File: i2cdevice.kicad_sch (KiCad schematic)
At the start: 46 parts, among them J29 6x2.54mm, J30 6x2.54mm, J31 6x2.54mm, J32 6x2.54mm, U10 INA219AxD, U11 MCP4725xxx-xCH, U12 24LC32

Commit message: First try to fit electronic on PCB
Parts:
- removed TP189: TestPoint_Small, Connector_PinHeader_2.54mm:PinHeader_1x01_P2.54mm_Horizontal, symbol Connector:TestPoint_Small
- TP100: renamed from TP215; footprint Connector_PinHeader_2.54mm:PinHeader_1x01_P2.54mm_Horizontal -> Connector_Pin:Pin_D1.0mm_L10.0mm
- TP101: renamed from TP216; footprint Connector_PinHeader_2.54mm:PinHeader_1x01_P2.54mm_Horizontal -> Connector_Pin:Pin_D1.0mm_L10.0mm
- U10: footprint Package_SO:SOIC-8_3.9x4.9mm_P1.27mm -> Package_TO_SOT_SMD:SOT-23-8; symbol Analog_ADC:INA219AxD -> Analog_ADC:INA219AxDCN
- renumbered J29 to J30, J30 to J31, J31 to J32, J32 to J33, NT459 to NT471, NT460 to NT472, NT461 to NT473, NT462 to NT474, NT463 to NT475, NT464 to NT476, NT465 to NT477, NT466 to NT478, NT467 to NT479, NT468 to NT480, NT469 to NT481, NT470 to NT482, NT471 to NT483, NT472 to NT484, NT473 to NT485, NT474 to NT486, NT475 to NT487, NT586 to NT488, NT476 to NT489, NT587 to NT490, NT477 to NT491, NT478 to NT492, NT479 to NT493, R86 to R73, R87 to R74, R88 to R75, R89 to R76, R90 to R77, R91 to R78, R92 to R79, R93 to R80, R94 to R81, R95 to R82, R96 to R83
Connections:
- net GND: now also U10.3 (GND); no longer U10.6 (GND)
- net I2C0_SCL: now also NT473.1; no longer NT471.1
- net I2C0_SDA: now also NT471.1; no longer NT473.1
- net I_SCL: now also NT473.2, R73.1, U10.5 (SCL); no longer NT471.2, R74.1, U10.3 (SDA)
- net I_SDA: now also NT471.2, R74.1, U10.6 (SDA); no longer NT473.2, R73.1, U10.4 (SCL)
- net VCC: now also U10.4 (VS); no longer U10.5 (VS)
- net VIN+: now also U10.1 (IN+); no longer U10.8 (IN+)
- net VIN-: now also U10.2 (IN-); no longer U10.7 (IN-)
- net at R79.1, R82.2: now also U10.7 (A0); no longer U10.2 (A0)
- net at R78.1, R81.2: now also U10.8 (A1); no longer U10.1 (A1)

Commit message: backup 1 bank done
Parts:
- NT471, NT472, NT473, NT474, NT475, NT476, NT477, NT478, NT479, NT480, NT481, NT482, NT483, NT484, NT485, NT486, NT487, NT488, NT489, NT490, NT491, NT492, NT493: footprint NetTie:NetTie-2_THT_Pad1.0mm -> NetTie:NetTie-2_Front1.0mm
- TP100, TP101: footprint Connector_Pin:Pin_D1.0mm_L10.0mm -> Connector_Pin:Pin_D0.9mm_L10.0mm_W2.4mm_FlatFork
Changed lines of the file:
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@@
     (property "Reference" "NT476" (id 0) (at 248.92 58.42 0))
     (property "Value" "I_INH" (id 1) (at 248.92 60.96 0))
-    (property "Footprint" "NetTie:NetTie-2_THT_Pad1.0mm" (id 2) (at 248.92 59.69 0)
+    (property "Footprint" "NetTie:NetTie-2_Front1.0mm" (id 2) (at 248.92 59.69 0)
       (effects (font (size 1.27 1.27)) hide)
     )
@@
     (property "Reference" "NT485" (id 0) (at 116.84 140.97 0))
     (property "Value" "C_M2" (id 1) (at 116.84 143.51 0))
-    (property "Footprint" "NetTie:NetTie-2_THT_Pad1.0mm" (id 2) (at 116.84 142.24 0)
+    (property "Footprint" "NetTie:NetTie-2_Front1.0mm" (id 2) (at 116.84 142.24 0)
       (effects (font (size 1.27 1.27)) hide)
     )
@@
     (property "Reference" "NT481" (id 0) (at 107.95 138.43 0))
     (property "Value" "C_M1" (id 1) (at 107.95 140.97 0))
-    (property "Footprint" "NetTie:NetTie-2_THT_Pad1.0mm" (id 2) (at 107.95 139.7 0)
+    (property "Footprint" "NetTie:NetTie-2_Front1.0mm" (id 2) (at 107.95 139.7 0)
       (effects (font (size 1.27 1.27)) hide)
     )
@@
     (property "Reference" "NT492" (id 0) (at 52.07 148.59 0))
     (property "Value" "C_VCC" (id 1) (at 52.07 151.13 0))
-    (property "Footprint" "NetTie:NetTie-2_THT_Pad1.0mm" (id 2) (at 52.07 149.86 0)
+    (property "Footprint" "NetTie:NetTie-2_Front1.0mm" (id 2) (at 52.07 149.86 0)
       (effects (font (size 1.27 1.27)) hide)
     )
@@
     (property "Reference" "NT474" (id 0) (at 179.07 55.88 0))
     (property "Value" "D_SDA" (id 1) (at 179.07 58.42 0))
-    (property "Footprint" "NetTie:NetTie-2_THT_Pad1.0mm" (id 2) (at 179.07 57.15 0)
+    (property "Footprint" "NetTie:NetTie-2_Front1.0mm" (id 2) (at 179.07 57.15 0)
       (effects (font (size 1.27 1.27)) hide)
     )
@@
     (property "Reference" "NT480" (id 0) (at 50.8 138.43 0))
     (property "Value" "C_SDA" (id 1) (at 50.8 140.97 0))
-    (property "Footprint" "NetTie:NetTie-2_THT_Pad1.0mm" (id 2) (at 50.8 139.7 0)
+    (property "Footprint" "NetTie:NetTie-2_Front1.0mm" (id 2) (at 50.8 139.7 0)
       (effects (font (size 1.27 1.27)) hide)
     )
@@
     (property "Reference" "NT491" (id 0) (at 116.84 146.05 0))
     (property "Value" "C_M4" (id 1) (at 116.84 148.59 0))
-    (property "Footprint" "NetTie:NetTie-2_THT_Pad1.0mm" (id 2) (at 116.84 147.32 0)
+    (property "Footprint" "NetTie:NetTie-2_Front1.0mm" (id 2) (at 116.84 147.32 0)
       (effects (font (size 1.27 1.27)) hide)
     )
@@
     (property "Reference" "NT477" (id 0) (at 127 62.23 0))
     (property "Value" "I_INL" (id 1) (at 127 64.77 0))
-    (property "Footprint" "NetTie:NetTie-2_THT_Pad1.0mm" (id 2) (at 127 63.5 0)
+    (property "Footprint" "NetTie:NetTie-2_Front1.0mm" (id 2) (at 127 63.5 0)
       (effects (font (size 1.27 1.27)) hide)
     )
@@
     (property "Reference" "NT482" (id 0) (at 200.66 138.43 0))
     (property "Value" "EE_A1" (id 1) (at 200.66 140.97 0))
-    (property "Footprint" "NetTie:NetTie-2_THT_Pad1.0mm" (id 2) (at 200.66 139.7 0)
+    (property "Footprint" "NetTie:NetTie-2_Front1.0mm" (id 2) (at 200.66 139.7 0)
       (effects (font (size 1.27 1.27)) hide)
     )
@@
     (property "Reference" "NT493" (id 0) (at 60.96 151.13 0))
     (property "Value" "C_GND" (id 1) (at 60.96 153.67 0))
-    (property "Footprint" "NetTie:NetTie-2_THT_Pad1.0mm" (id 2) (at 60.96 152.4 0)
+    (property "Footprint" "NetTie:NetTie-2_Front1.0mm" (id 2) (at 60.96 152.4 0)
       (effects (font (size 1.27 1.27)) hide)
     )
@@
     (property "Reference" "NT471" (id 0) (at 44.45 53.34 0))
     (property "Value" "I_SDA" (id 1) (at 44.45 55.88 0))
-    (property "Footprint" "NetTie:NetTie-2_THT_Pad1.0mm" (id 2) (at 44.45 54.61 0)
+    (property "Footprint" "NetTie:NetTie-2_Front1.0mm" (id 2) (at 44.45 54.61 0)
       (effects (font (size 1.27 1.27)) hide)
     )
@@
     (property "Reference" "NT484" (id 0) (at 43.18 140.97 0))
     (property "Value" "C_SCL" (id 1) (at 43.18 143.51 0))
-    (property "Footprint" "NetTie:NetTie-2_THT_Pad1.0mm" (id 2) (at 43.18 142.24 0)
+    (property "Footprint" "NetTie:NetTie-2_Front1.0mm" (id 2) (at 43.18 142.24 0)
       (effects (font (size 1.27 1.27)) hide)
     )
@@
     (property "Reference" "NT479" (id 0) (at 232.41 135.89 0))
     (property "Value" "EE_SDA" (id 1) (at 232.41 138.43 0))
-    (property "Footprint" "NetTie:NetTie-2_THT_Pad1.0mm" (id 2) (at 232.41 137.16 0)
+    (property "Footprint" "NetTie:NetTie-2_Front1.0mm" (id 2) (at 232.41 137.16 0)
       (effects (font (size 1.27 1.27)) hide)
     )
@@
       (effects (font (size 1.27 1.27)) (justify left) hide)
     )
-    (property "Footprint" "Connector_Pin:Pin_D1.0mm_L10.0mm" (id 2) (at 113.03 157.48 0)
+    (property "Footprint" "Connector_Pin:Pin_D0.9mm_L10.0mm_W2.4mm_FlatFork" (id 2) (at 113.03 157.48 0)
       (effects (font (size 1.27 1.27)) hide)
     )
@@
     (property "Reference" "NT489" (id 0) (at 107.95 143.51 0))
     (property "Value" "C_M3" (id 1) (at 107.95 146.05 0))
-    (property "Footprint" "NetTie:NetTie-2_THT_Pad1.0mm" (id 2) (at 107.95 144.78 0)
+    (property "Footprint" "NetTie:NetTie-2_Front1.0mm" (id 2) (at 107.95 144.78 0)
       (effects (font (size 1.27 1.27)) hide)
     )
@@
     (property "Reference" "NT490" (id 0) (at 43.18 146.05 0))
     (property "Value" "C_4" (id 1) (at 43.18 148.59 0))
-    (property "Footprint" "NetTie:NetTie-2_THT_Pad1.0mm" (id 2) (at 43.18 147.32 0)
+    (property "Footprint" "NetTie:NetTie-2_Front1.0mm" (id 2) (at 43.18 147.32 0)
       (effects (font (size 1.27 1.27)) hide)
     )
@@
     (property "Reference" "NT488" (id 0) (at 50.8 143.51 0))
     (property "Value" "C_3" (id 1) (at 50.8 146.05 0))
-    (property "Footprint" "NetTie:NetTie-2_THT_Pad1.0mm" (id 2) (at 50.8 144.78 0)
+    (property "Footprint" "NetTie:NetTie-2_Front1.0mm" (id 2) (at 50.8 144.78 0)
       (effects (font (size 1.27 1.27)) hide)
     )
@@
     (property "Reference" "NT478" (id 0) (at 191.77 135.89 0))
     (property "Value" "EE_A0" (id 1) (at 191.77 138.43 0))
-    (property "Footprint" "NetTie:NetTie-2_THT_Pad1.0mm" (id 2) (at 191.77 137.16 0)
+    (property "Footprint" "NetTie:NetTie-2_Front1.0mm" (id 2) (at 191.77 137.16 0)
       (effects (font (size 1.27 1.27)) hide)
     )
@@
     (property "Reference" "NT487" (id 0) (at 233.68 140.97 0))
     (property "Value" "EE_A2" (id 1) (at 233.68 143.51 0))
-    (property "Footprint" "NetTie:NetTie-2_THT_Pad1.0mm" (id 2) (at 233.68 142.24 0)
+    (property "Footprint" "NetTie:NetTie-2_Front1.0mm" (id 2) (at 233.68 142.24 0)
       (effects (font (size 1.27 1.27)) hide)
     )
@@
     (property "Reference" "NT475" (id 0) (at 171.45 58.42 0))
     (property "Value" "D_SCL" (id 1) (at 171.45 60.96 0))
-    (property "Footprint" "NetTie:NetTie-2_THT_Pad1.0mm" (id 2) (at 171.45 59.69 0)
+    (property "Footprint" "NetTie:NetTie-2_Front1.0mm" (id 2) (at 171.45 59.69 0)
       (effects (font (size 1.27 1.27)) hide)
     )
@@
     (property "Reference" "NT473" (id 0) (at 36.83 55.88 0))
     (property "Value" "I_SCL" (id 1) (at 36.83 58.42 0))
-    (property "Footprint" "NetTie:NetTie-2_THT_Pad1.0mm" (id 2) (at 36.83 57.15 0)
+    (property "Footprint" "NetTie:NetTie-2_Front1.0mm" (id 2) (at 36.83 57.15 0)
       (effects (font (size 1.27 1.27)) hide)
     )
@@
     (property "Reference" "NT483" (id 0) (at 240.03 138.43 0))
     (property "Value" "EE_SCL" (id 1) (at 240.03 140.97 0))
-    (property "Footprint" "NetTie:NetTie-2_THT_Pad1.0mm" (id 2) (at 240.03 139.7 0)
+    (property "Footprint" "NetTie:NetTie-2_Front1.0mm" (id 2) (at 240.03 139.7 0)
       (effects (font (size 1.27 1.27)) hide)
     )
@@
       (effects (font (size 1.27 1.27)) (justify left) hide)
     )
-    (property "Footprint" "Connector_Pin:Pin_D1.0mm_L10.0mm" (id 2) (at 113.03 152.4 0)
+    (property "Footprint" "Connector_Pin:Pin_D0.9mm_L10.0mm_W2.4mm_FlatFork" (id 2) (at 113.03 152.4 0)
       (effects (font (size 1.27 1.27)) hide)
     )
@@
     (property "Reference" "NT472" (id 0) (at 127 54.61 0))
     (property "Value" "I_INH" (id 1) (at 127 57.15 0))
-    (property "Footprint" "NetTie:NetTie-2_THT_Pad1.0mm" (id 2) (at 127 55.88 0)
+    (property "Footprint" "NetTie:NetTie-2_Front1.0mm" (id 2) (at 127 55.88 0)
       (effects (font (size 1.27 1.27)) hide)
     )
@@
     (property "Reference" "NT486" (id 0) (at 191.77 140.97 0))
     (property "Value" "EE_A2" (id 1) (at 191.77 143.51 0))
-    (property "Footprint" "NetTie:NetTie-2_THT_Pad1.0mm" (id 2) (at 191.77 142.24 0)
-      (effects (font (size 1.27 1.27)) hide)
-    )
+    (property "Footprint" "NetTie:NetTie-2_Front1.0mm" (id 2) (at 191.77 142.24 0)
+      (effects (font (size 1.27 1.27)) hide)
+    )

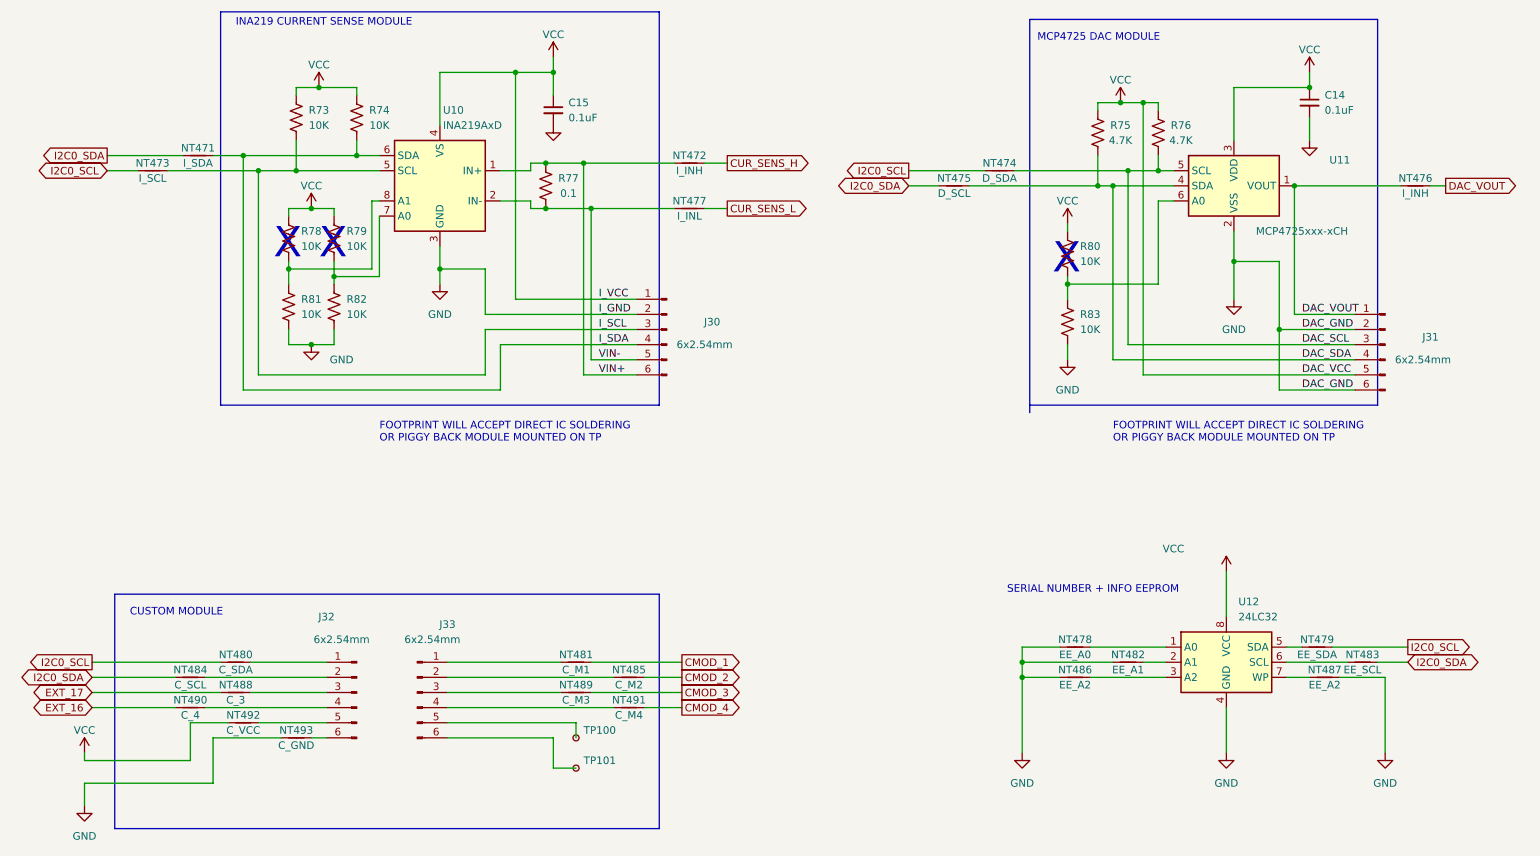
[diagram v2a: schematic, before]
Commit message: PCB Completed
PCB completed but final verification not completed
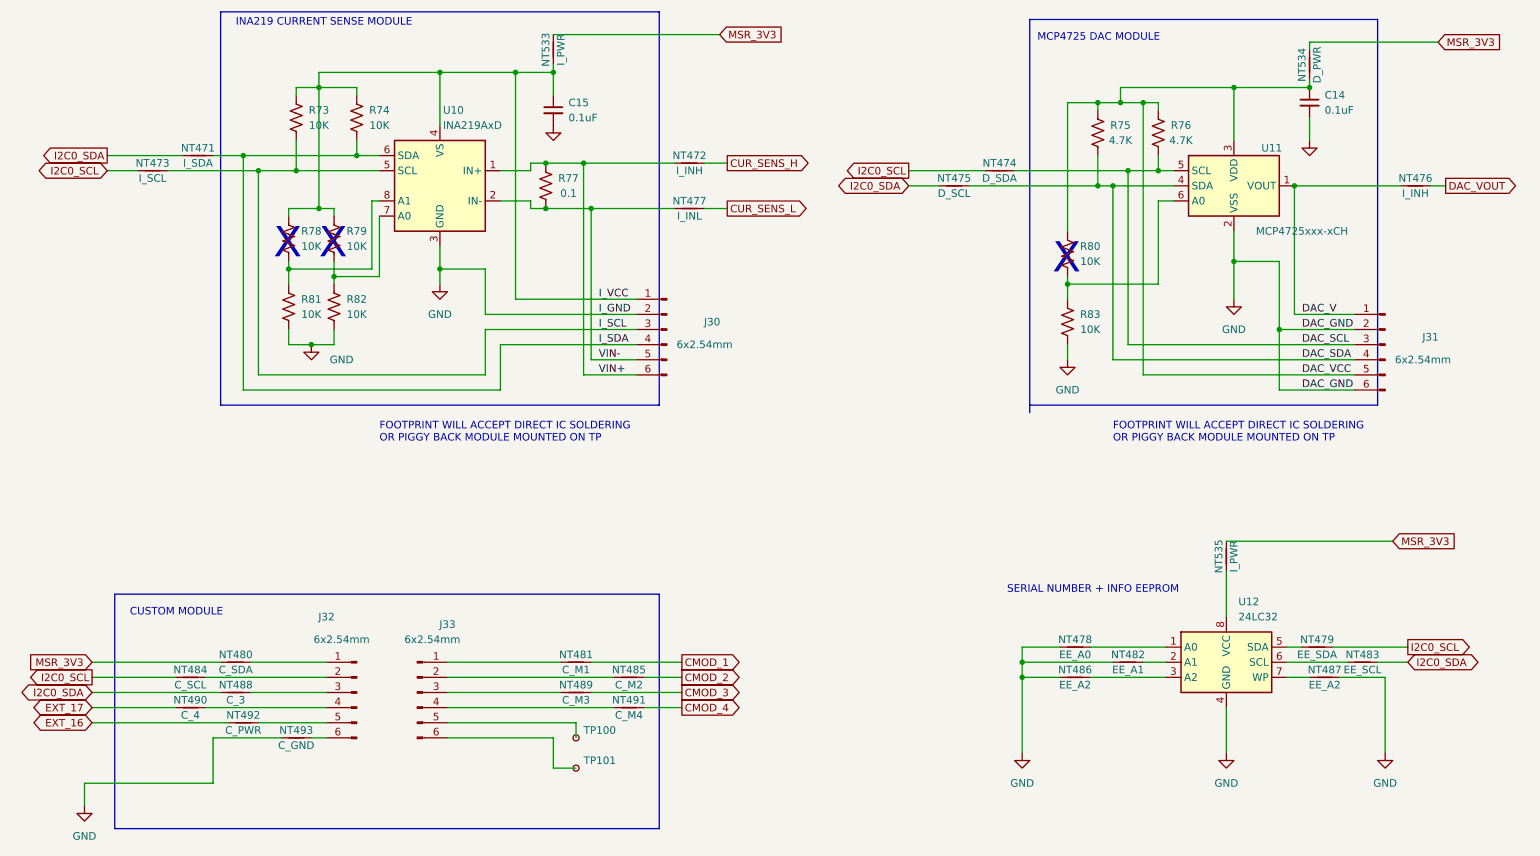
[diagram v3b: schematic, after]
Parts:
- added NT533, NT535: I_PWR, NetTie:NetTie-2_Front1.0mm, symbol Device:NetTie_2
- added NT534: D_PWR, NetTie:NetTie-2_Front1.0mm, symbol Device:NetTie_2
- J30, J31, J32, J33: footprint Connector_PinHeader_2.54mm:PinHeader_1x06_P2.54mm_Vertical -> Connector_PinSocket_2.54mm:PinSocket_1x06_P2.54mm_Vertical
- NT492: value C_VCC -> C_PWR
- TP100, TP101: footprint Connector_Pin:Pin_D0.9mm_L10.0mm_W2.4mm_FlatFork -> TestPoint:TestPoint_THTPad_D1.5mm_Drill0.7mm
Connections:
- net DAC_VOUT: no longer J31.1 (Pin_1), NT476.2, U11.1 (VOUT)
- net EXT_16: now also NT492.1; no longer NT490.1
- net EXT_17: now also NT490.1; no longer NT488.1
- net I2C0_SCL: now also NT484.1; no longer NT480.1
- net I2C0_SDA: now also NT488.1; no longer NT484.1
- removed net VCC: C14.1, C15.1, J30.1 (Pin_1), J31.5 (Pin_5), NT492.1, R73.2, R74.2, R75.2, R76.2, R78.2, R79.2, R80.2, U10.4 (VS), U11.3 (VDD), U12.8 (VCC)
- new net: NT535.1, U12.8 (VCC)
- new net DAC_V: J31.1 (Pin_1), NT476.2, U11.1 (VOUT)
- new net DAC_VCC: C14.1, J31.5 (Pin_5), NT534.1, R75.2, R76.2, R80.2, U11.3 (VDD)
- new net I_VCC: C15.1, J30.1 (Pin_1), NT533.1, R73.2, R74.2, R78.2, R79.2, U10.4 (VS)
- new net MSR_3V3: NT480.1, NT533.2, NT534.2, NT535.2

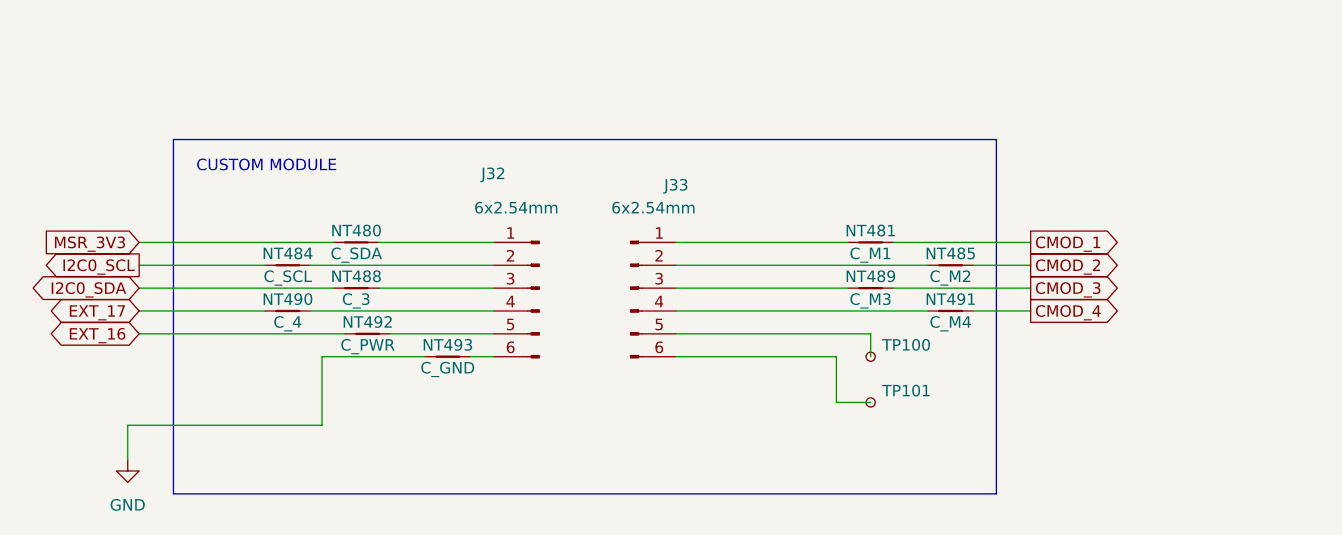
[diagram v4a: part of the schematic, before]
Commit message: Change custom connector
Use 8 pins to replace 6 pins
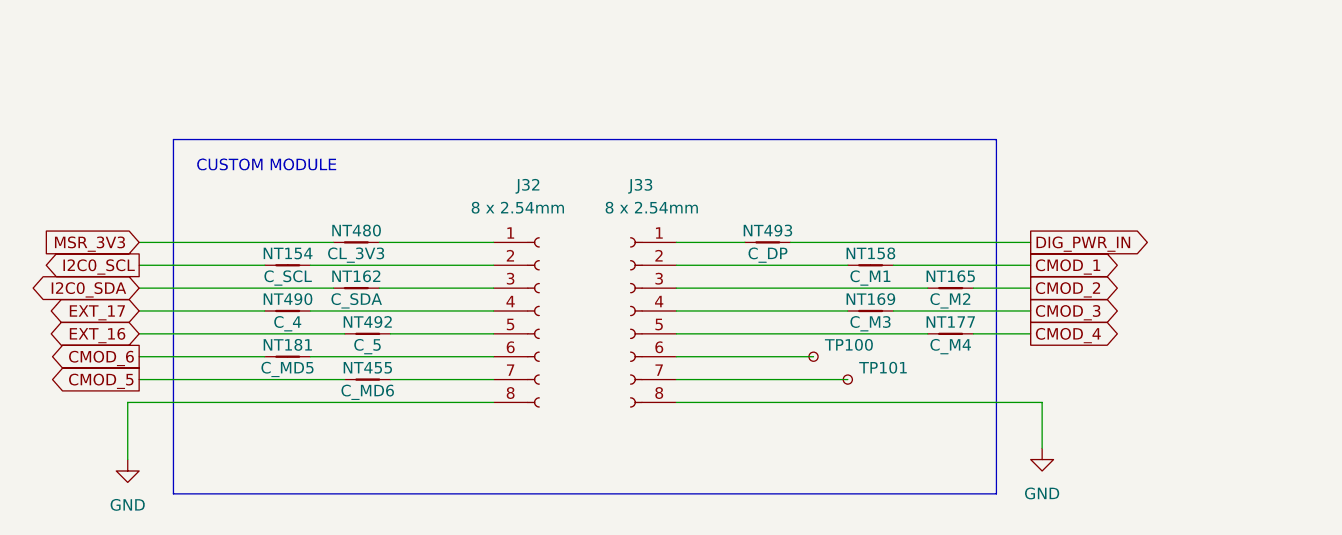
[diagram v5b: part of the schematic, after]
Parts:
- removed J32, J33: 6x2.54mm, Connector_PinSocket_2.54mm:PinSocket_1x06_P2.54mm_Vertical, symbol Connector:Conn_01x06_Male
- removed NT481: C_M1, NetTie:NetTie-2_Front1.0mm, symbol Device:NetTie_2
- removed NT484: C_SCL, NetTie:NetTie-2_Front1.0mm, symbol Device:NetTie_2
- removed NT485: C_M2, NetTie:NetTie-2_Front1.0mm, symbol Device:NetTie_2
- removed NT488: C_3, NetTie:NetTie-2_Front1.0mm, symbol Device:NetTie_2
- removed NT489: C_M3, NetTie:NetTie-2_Front1.0mm, symbol Device:NetTie_2
- removed NT491: C_M4, NetTie:NetTie-2_Front1.0mm, symbol Device:NetTie_2
- added J32, J33: 8 x 2.54mm, Connector_PinSocket_2.54mm:PinSocket_1x08_P2.54mm_Vertical, symbol Connector:Conn_01x08_Female
- added NT154: C_SCL, NetTie:NetTie-2_Front1.0mm, symbol Device:NetTie_2
- added NT158: C_M1, NetTie:NetTie-2_Front1.0mm, symbol Device:NetTie_2
- added NT162: C_SDA, NetTie:NetTie-2_Front1.0mm, symbol Device:NetTie_2
- added NT165: C_M2, NetTie:NetTie-2_Front1.0mm, symbol Device:NetTie_2
- added NT169: C_M3, NetTie:NetTie-2_Front1.0mm, symbol Device:NetTie_2
- added NT177: C_M4, NetTie:NetTie-2_Front1.0mm, symbol Device:NetTie_2
- added NT181: C_MD5, NetTie:NetTie-2_Front1.0mm, symbol Device:NetTie_2
- added NT455: C_MD6, NetTie:NetTie-2_Front1.0mm, symbol Device:NetTie_2
- NT480: value C_SDA -> CL_3V3
- NT492: value C_PWR -> C_5
- NT493: value C_GND -> C_DP
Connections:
- net CMOD_1: now also NT158.2
- net CMOD_2: now also NT165.2
- net CMOD_3: now also NT169.2
- net CMOD_4: now also NT177.2
- net GND: now also J32.8 (Pin_8), J33.8 (Pin_8); no longer NT493.1
- net I2C0_SCL: now also NT154.1
- net I2C0_SDA: now also NT162.1
- net at NT492.2: now also J32.5 (Pin_5)
- net at NT480.2: now also J32.1 (Pin_1)
- net DIG_PWR_IN: now reaches NT493.2
- net at TP101.1: now also J33.7 (Pin_7)
- net at NT490.2: now also J32.4 (Pin_4)
- net at TP100.1: now also J33.6 (Pin_6)
- new net: J32.2 (Pin_2), NT154.2
- new net: J32.3 (Pin_3), NT162.2
- new net: J32.6 (Pin_6), NT181.1
- new net: J32.7 (Pin_7), NT455.1
- new net: J33.3 (Pin_3), NT165.1
- new net: J33.2 (Pin_2), NT158.1
- new net: J33.1 (Pin_1), NT493.1
- new net: J33.4 (Pin_4), NT169.1
- new net: J33.5 (Pin_5), NT177.1
- new net CMOD_5: NT455.2
- new net CMOD_6: NT181.2
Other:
- moved on the sheet: NT493, TP100, TP101

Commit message: update
Correction of small error
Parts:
- added R8, R9: 10K, Resistor_THT:R_Axial_DIN0207_L6.3mm_D2.5mm_P10.16mm_Horizontal, symbol Device:R_US
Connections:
- net I2C0_SCL: now also NT483.1; no longer NT479.1
- net I2C0_SDA: now also NT479.1; no longer NT483.1
- net MSR_3V3: now also R8.2, R9.2
- net at NT479.2, U12.5 (SDA): now also R8.1
- net at NT483.2, U12.6 (SCL): now also R9.1
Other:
- moved on the sheet: NT479, NT483, R73
